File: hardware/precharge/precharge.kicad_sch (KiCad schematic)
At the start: 31 parts, among them J1 Conn_01x02, J2 Conn_01x01, J3 Conn_01x05, J4 Conn_01x04, J5 Conn_01x01, K1 DIPxx-1Cxx-51x, U1 140817141410, U2 140817141410, U3 140817141410

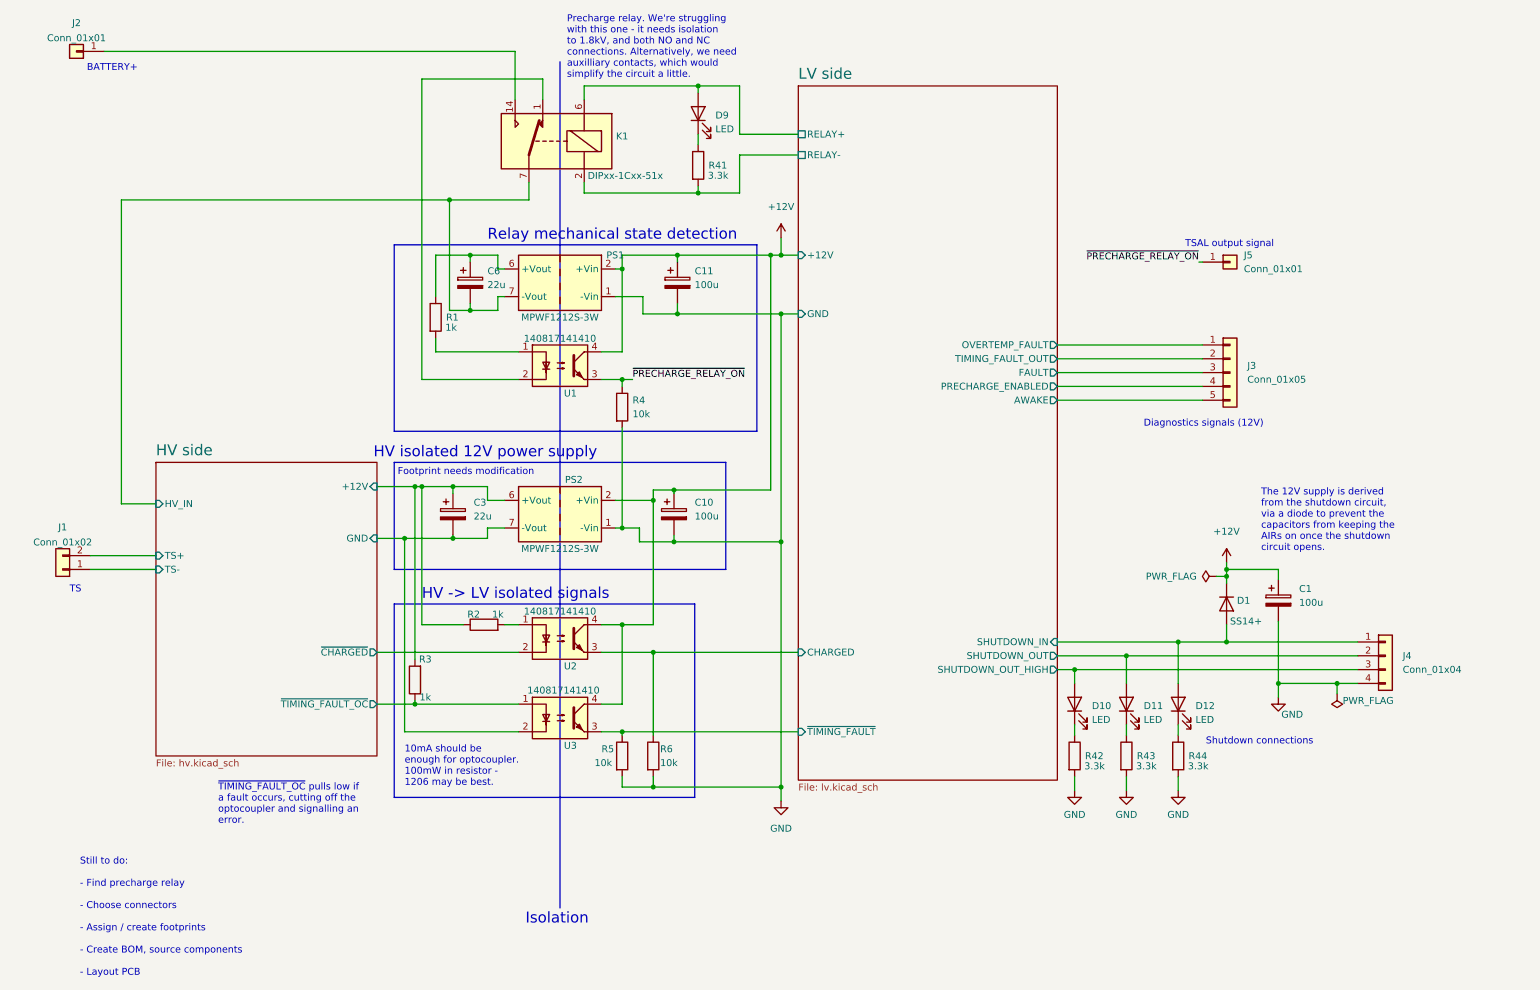
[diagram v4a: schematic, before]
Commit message: Added support for TS_ACTIVE signal, adjusted resistor divider
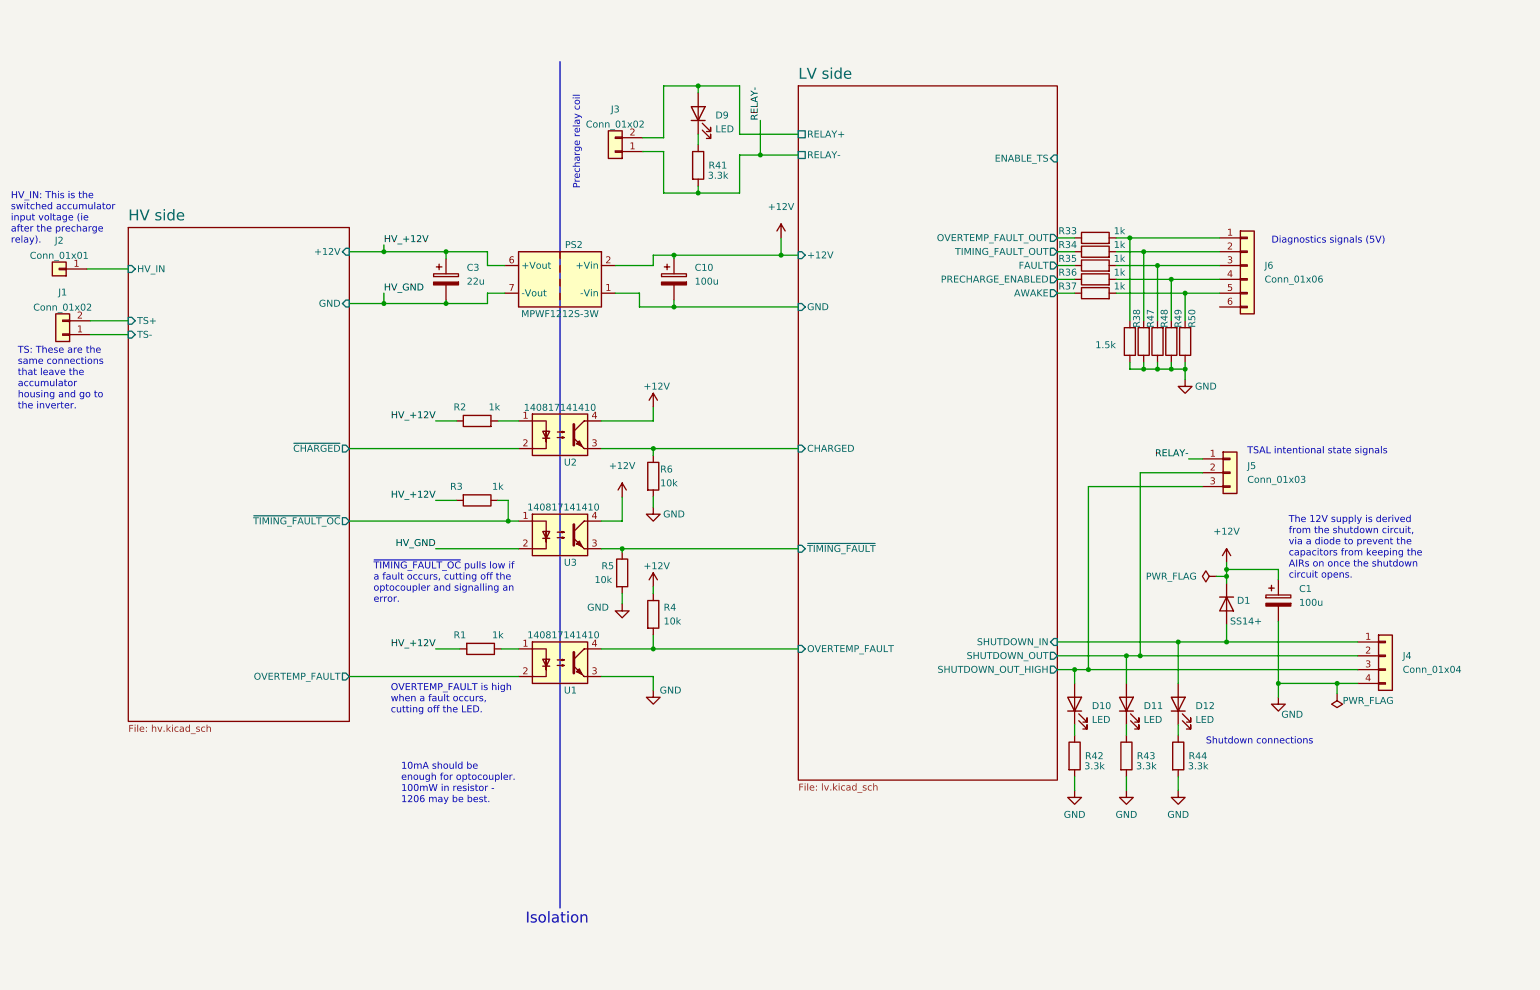
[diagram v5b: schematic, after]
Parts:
- removed C11: 100u, Capacitor_THT:CP_Radial_D6.3mm_P2.50mm, symbol Device:C_Polarized
- removed C6: 22u, Capacitor_THT:CP_Radial_D8.0mm_P3.50mm, symbol Device:C_Polarized
- removed J3: Conn_01x05, Connector_PinHeader_2.54mm:PinHeader_1x05_P2.54mm_Horizontal, symbol Connector_Generic:Conn_01x05
- removed J5: Conn_01x01, Connector_PinHeader_2.54mm:PinHeader_1x01_P2.54mm_Horizontal, symbol Connector_Generic:Conn_01x01
- removed K1: DIPxx-1Cxx-51x, Relay_THT:Relay_StandexMeder_DIP_LowProfile, symbol Relay:DIPxx-1Cxx-51x
- removed PS1: MPWF1212S-3W, Converter_DCDC:Converter_DCDC_XP_POWER-ITXxxxxSA_THT, symbol Converter_DCDC:ITX1212SA
- added J3: Conn_01x02, Connector_PinHeader_2.54mm:PinHeader_1x02_P2.54mm_Horizontal, symbol Connector_Generic:Conn_01x02
- added J5: Conn_01x03, Connector_PinHeader_2.54mm:PinHeader_1x03_P2.54mm_Horizontal, symbol Connector_Generic:Conn_01x03
- added J6: Conn_01x06, Connector_PinHeader_2.54mm:PinHeader_1x06_P2.54mm_Horizontal, symbol Connector_Generic:Conn_01x06
- added R33, R34, R35, R36, R37: 1k, Resistor_SMD:R_0603_1608Metric, symbol Device:R
- added R38, R47, R48, R49, R50: 1.5k, Resistor_SMD:R_0603_1608Metric, symbol Device:R
- R1: footprint Resistor_SMD:R_0603_1608Metric -> Resistor_SMD:R_1206_3216Metric; Power 2W -> (none)
- R2, R3: footprint Resistor_SMD:R_0603_1608Metric -> Resistor_SMD:R_1206_3216Metric
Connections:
- net HV side/+12V is gone; now on net HV_+12V: C3.1, PS2.6 (+Vout), R2.1, R3.2
- net +12V: now also R4.1; no longer U1.4
- net GND: now also U1.3, R38.1, R47.1, R48.1, R49.1, R50.1; no longer C10.2, PS2.1 (-Vin), R4.2
- net HV side/HV_IN: now also J2.1 (Pin_1)
- net LV side/AWAKE: now also R37.1
- net LV side/FAULT: now also R35.1
- net LV side/OVERTEMP_FAULT: now also R4.2, U1.4
- net LV side/PRECHARGE_ENABLED: now also R36.1
- net LV side/RELAY+: now also J3.2 (Pin_2)
- net LV side/SHUTDOWN_OUT: now also J5.2 (Pin_2)
- net LV side/SHUTDOWN_OUT_HIGH: now also J5.3 (Pin_3)
- net LV side/TIMING_FAULT_OUT: now also R34.1
- net at R1.1: now also U1.1
- net HV_+12V: now reaches R1.2
- net HV_+12V: no longer U1.1
- net HV side/OVERTEMP_FAULT: now reaches U1.2
- net HV side/GND renamed HV_GND
- net LV side/RELAY- renamed RELAY-
- net RELAY-: now also J3.1 (Pin_1), J5.1 (Pin_1)
- removed net ~{PRECHARGE_RELAY_ON}: R4.1, U1.3
- new net: J6.1 (Pin_1), R33.2, R38.2
- new net: J6.4 (Pin_4), R36.2, R49.2
- new net: J6.2 (Pin_2), R34.2, R47.2
- new net: J6.3 (Pin_3), R35.2, R48.2
- new net: J6.5 (Pin_5), R37.2, R50.2
- new net LV side/GND: C10.2, PS2.1 (-Vin)
- new net LV side/OVERTEMP_FAULT_OUT: R33.1
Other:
- sheet HV side ports: added OVERTEMP_FAULT; removed none
- sheet LV side ports: added ENABLE_TS, OVERTEMP_FAULT_OUT; removed none
- note added: "Diagnostics signals (5V)"
- note added: "HV_IN: This is the switched accumulator input voltage (ie after the precharge relay)."
- note added: "OVERTEMP_FAULT is high when a fault occurs, cutting off the LED."
- note added: "Precharge relay coil"
- note added: "TS: These are the same connections that leave the accumulator housing and go to the inverter."
- note added: "TSAL intentional state signals"
- note removed: "BATTERY+"
- note removed: "Diagnostics signals (12V)"
- note removed: "Footprint needs modification"
- note removed: "HV -> LV isolated signals"
- note removed: "HV isolated 12V power supply"
- note removed: "Precharge relay. We're struggling with this one - it needs isolation to 1.8kV, and both NO and NC connections. Alternatively, we need auxilliary contacts, which would simplify the circuit a little."
- note removed: "Relay mechanical state detection"
- note removed: "Still to do: - Find precharge relay - Choose connectors - Assign / create footprints - Create BOM, source components - Layout PCB"
- note removed: "TS"
- note removed: "TSAL output signal"
- moved on the sheet: C10, C3, J1, J2, PS2, R2, R3, R5, R6, U2, U3

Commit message: ??
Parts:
- removed J2: Conn_01x01, Connector_PinHeader_2.54mm:PinHeader_1x01_P2.54mm_Horizontal, symbol Connector_Generic:Conn_01x01
- removed J6: Conn_01x06, Connector_PinHeader_2.54mm:PinHeader_1x06_P2.54mm_Horizontal, symbol Connector_Generic:Conn_01x06
- added J2: Conn_01x02, Connector_Molex:Molex_Micro-Fit_3.0_43650-0200_1x02_P3.00mm_Horizontal, symbol Connector_Generic:Conn_01x02
- added J6: Conn_01x05, Connector_Molex:Molex_Micro-Fit_3.0_43650-0500_1x05_P3.00mm_Horizontal, symbol Connector_Generic:Conn_01x05
- J1, J3: footprint Connector_PinHeader_2.54mm:PinHeader_1x02_P2.54mm_Horizontal -> Connector_Molex:Molex_Micro-Fit_3.0_43650-0200_1x02_P3.00mm_Horizontal
- J4: footprint Connector_PinHeader_2.54mm:PinHeader_1x04_P2.54mm_Horizontal -> Connector_Molex:Molex_Micro-Fit_3.0_43650-0400_1x04_P3.00mm_Horizontal
- J5: footprint Connector_PinHeader_2.54mm:PinHeader_1x03_P2.54mm_Horizontal -> Connector_Molex:Molex_Micro-Fit_3.0_43650-0300_1x03_P3.00mm_Horizontal
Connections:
- net HV side/HV_IN: now also J2.1 (Pin_1), J2.2 (Pin_2)
- net at R33.2, R38.2: now also J6.1 (Pin_1)
- net at R36.2, R49.2: now also J6.4 (Pin_4)
- net at R34.2, R47.2: now also J6.2 (Pin_2)
- net at R35.2, R48.2: now also J6.3 (Pin_3)
- net at R37.2, R50.2: now also J6.5 (Pin_5)
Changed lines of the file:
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@@
   (junction (at 134.62 130.81) (diameter 0) (color 0 0 0 0)
+  )
+  (junction (at 31.75 60.96) (diameter 0) (color 0 0 0 0)
   )
   (junction (at 222.25 55.245) (diameter 0) (color 0 0 0 0)
@@
     (stroke (width 0) (type default) (color 0 0 0 0))
   )
+  (wire (pts (xy 30.48 58.42) (xy 31.75 58.42))
+    (stroke (width 0) (type default) (color 0 0 0 0))
+  )
   (wire (pts (xy 138.43 67.945) (xy 161.29 67.945))
     (stroke (width 0) (type default) (color 0 0 0 0))
@@
     (stroke (width 0) (type default) (color 0 0 0 0))
   )
-  (wire (pts (xy 30.48 60.96) (xy 38.1 60.96))
+  (wire (pts (xy 30.48 60.96) (xy 31.75 60.96))
     (stroke (width 0) (type default) (color 0 0 0 0))
   )
@@
     (stroke (width 0) (type default) (color 0 0 0 0))
   )
+  (wire (pts (xy 31.75 58.42) (xy 31.75 60.96))
+    (stroke (width 0) (type default) (color 0 0 0 0))
+  )
   (polyline (pts (xy 116.84 46.355) (xy 116.84 46.355))
     (stroke (width 0) (type default) (color 0 0 0 0))
@@
   )
   (wire (pts (xy 227.33 60.325) (xy 238.76 60.325))
+    (stroke (width 0) (type default) (color 0 0 0 0))
+  )
+  (wire (pts (xy 31.75 60.96) (xy 38.1 60.96))
     (stroke (width 0) (type default) (color 0 0 0 0))
   )
@@
   )
   (text "HV_IN: This is the\nswitched accumulator\ninput voltage (ie \nafter the precharge\nrelay)."
-    (at 16.51 56.515 0)
+    (at 16.51 48.895 0)
     (effects (font (size 1.27 1.27)) (justify left bottom))
   )
@@
     (pin "2")
   )
+  (symbol (lib_id "Connector_Generic:Conn_01x05") (at 243.84 60.325 0) (unit 1)
+    (in_bom yes) (on_board yes) (fields_autoplaced)
+    (property "Reference" "J6" (id 0) (at 246.38 59.0549 0)
+      (effects (font (size 1.27 1.27)) (justify left))
+    )
+    (property "Value" "Conn_01x05" (id 1) (at 246.38 61.5949 0)
+      (effects (font (size 1.27 1.27)) (justify left))
+    )
+    (property "Footprint" "Connector_Molex:Molex_Micro-Fit_3.0_43650-0500_1x05_P3.00mm_Horizontal" (id 2) (at 243.84 60.325 0)
+      (effects (font (size 1.27 1.27)) hide)
+    )
+    (property "Datasheet" "~" (id 3) (at 243.84 60.325 0)
+      (effects (font (size 1.27 1.27)) hide)
+    )
+    (pin "1")
+    (pin "2")
+    (pin "3")
+    (pin "4")
+    (pin "5")
+  )
   (symbol (lib_id "Device:R") (at 212.09 150.495 0) (unit 1)
     (in_bom yes) (on_board yes)
@@
     (pin "2")
   )
-  (symbol (lib_id "Connector_Generic:Conn_01x06") (at 243.84 60.325 0) (unit 1)
-    (in_bom yes) (on_board yes) (fields_autoplaced)
-    (property "Reference" "J6" (id 0) (at 247.015 60.3249 0)
-      (effects (font (size 1.27 1.27)) (justify left))
-    )
-    (property "Value" "Conn_01x06" (id 1) (at 247.015 62.8649 0)
-      (effects (font (size 1.27 1.27)) (justify left))
-    )
-    (property "Footprint" "Connector_PinHeader_2.54mm:PinHeader_1x06_P2.54mm_Horizontal" (id 2) (at 243.84 60.325 0)
-      (effects (font (size 1.27 1.27)) hide)
-    )
-    (property "Datasheet" "~" (id 3) (at 243.84 60.325 0)
-      (effects (font (size 1.27 1.27)) hide)
-    )
-    (pin "1")
-    (pin "2")
-    (pin "3")
-    (pin "4")
-    (pin "5")
-    (pin "6")
+  (symbol (lib_id "Connector_Generic:Conn_01x02") (at 25.4 60.96 180) (unit 1)
+    (in_bom yes) (on_board yes) (fields_autoplaced)
+    (property "Reference" "J2" (id 0) (at 25.4 51.435 0))
+    (property "Value" "Conn_01x02" (id 1) (at 25.4 53.975 0))
+    (property "Footprint" "Connector_Molex:Molex_Micro-Fit_3.0_43650-0200_1x02_P3.00mm_Horizontal" (id 2) (at 25.4 60.96 0)
+      (effects (font (size 1.27 1.27)) hide)
+    )
+    (property "Datasheet" "~" (id 3) (at 25.4 60.96 0)
+      (effects (font (size 1.27 1.27)) hide)
+    )
+    (pin "1")
+    (pin "2")
   )
   (symbol (lib_id "power:+12V") (at 128.905 102.87 0) (unit 1)
@@
       (effects (font (size 1.27 1.27)) (justify left))
     )
-    (property "Footprint" "Connector_PinHeader_2.54mm:PinHeader_1x04_P2.54mm_Horizontal" (id 2) (at 269.24 132.08 0)
+    (property "Footprint" "Connector_Molex:Molex_Micro-Fit_3.0_43650-0400_1x04_P3.00mm_Horizontal" (id 2) (at 269.24 132.08 0)
       (effects (font (size 1.27 1.27)) hide)
     )
@@
     (pin "1")
   )
-  (symbol (lib_id "Connector_Generic:Conn_01x01") (at 25.4 60.96 180) (unit 1)
-    (in_bom yes) (on_board yes) (fields_autoplaced)
-    (property "Reference" "J2" (id 0) (at 25.4 55.7235 0))
-    (property "Value" "Conn_01x01" (id 1) (at 25.4 58.4986 0))
-    (property "Footprint" "Connector_PinHeader_2.54mm:PinHeader_1x01_P2.54mm_Horizontal" (id 2) (at 25.4 60.96 0)
-      (effects (font (size 1.27 1.27)) hide)
-    )
-    (property "Datasheet" "~" (id 3) (at 25.4 60.96 0)
-      (effects (font (size 1.27 1.27)) hide)
-    )
-    (pin "1")
-  )
   (symbol (lib_id "Device:C_Polarized") (at 96.52 62.865 0) (unit 1)
     (in_bom yes) (on_board yes) (fields_autoplaced)
@@
     (property "Reference" "J3" (id 0) (at 127.635 31.5935 0))
     (property "Value" "Conn_01x02" (id 1) (at 127.635 34.3686 0))
-    (property "Footprint" "Connector_PinHeader_2.54mm:PinHeader_1x02_P2.54mm_Horizontal" (id 2) (at 127.635 39.37 0)
+    (property "Footprint" "Connector_Molex:Molex_Micro-Fit_3.0_43650-0200_1x02_P3.00mm_Horizontal" (id 2) (at 127.635 39.37 0)
       (effects (font (size 1.27 1.27)) hide)
     )
@@
       (effects (font (size 1.27 1.27)) (justify left))
     )
-    (property "Footprint" "Connector_PinHeader_2.54mm:PinHeader_1x03_P2.54mm_Horizontal" (id 2) (at 240.665 98.425 0)
+    (property "Footprint" "Connector_Molex:Molex_Micro-Fit_3.0_43650-0300_1x03_P3.00mm_Horizontal" (id 2) (at 240.665 98.425 0)
       (effects (font (size 1.27 1.27)) hide)
     )
@@
     (property "Reference" "J1" (id 0) (at 26.035 65.2485 0))
     (property "Value" "Conn_01x02" (id 1) (at 26.035 68.0236 0))
-    (property "Footprint" "Connector_PinHeader_2.54mm:PinHeader_1x02_P2.54mm_Horizontal" (id 2) (at 26.035 73.025 0)
+    (property "Footprint" "Connector_Molex:Molex_Micro-Fit_3.0_43650-0200_1x02_P3.00mm_Horizontal" (id 2) (at 26.035 73.025 0)
       (effects (font (size 1.27 1.27)) hide)
     )
@@
     )
     (path "/c1d028f3-91e9-41f8-8563-411af756b606"
-      (reference "J1") (unit 1) (value "Conn_01x02") (footprint "Connector_PinHeader_2.54mm:PinHeader_1x02_P2.54mm_Horizontal")
-    )
-    (path "/9675ae6d-9635-4b89-ab4f-854f5484396b"
-      (reference "J2") (unit 1) (value "Conn_01x01") (footprint "Connector_PinHeader_2.54mm:PinHeader_1x01_P2.54mm_Horizontal")
+      (reference "J1") (unit 1) (value "Conn_01x02") (footprint "Connector_Molex:Molex_Micro-Fit_3.0_43650-0200_1x02_P3.00mm_Horizontal")
+    )
+    (path "/42f26f97-84ba-4654-93f0-c5bfb573e97d"
+      (reference "J2") (unit 1) (value "Conn_01x02") (footprint "Connector_Molex:Molex_Micro-Fit_3.0_43650-0200_1x02_P3.00mm_Horizontal")
     )
     (path "/ac2f3eb5-9193-4a6c-bab6-d1de91fe5122"
-      (reference "J3") (unit 1) (value "Conn_01x02") (footprint "Connector_PinHeader_2.54mm:PinHeader_1x02_P2.54mm_Horizontal")
+      (reference "J3") (unit 1) (value "Conn_01x02") (footprint "Connector_Molex:Molex_Micro-Fit_3.0_43650-0200_1x02_P3.00mm_Horizontal")
     )
     (path "/616c1ff6-bb93-43c9-a485-6175455d841d"
-      (reference "J4") (unit 1) (value "Conn_01x04") (footprint "Connector_PinHeader_2.54mm:PinHeader_1x04_P2.54mm_Horizontal")
+      (reference "J4") (unit 1) (value "Conn_01x04") (footprint "Connector_Molex:Molex_Micro-Fit_3.0_43650-0400_1x04_P3.00mm_Horizontal")
     )
     (path "/bec1f211-1161-41c0-a581-e039a5c66ab7"
-      (reference "J5") (unit 1) (value "Conn_01x03") (footprint "Connector_PinHeader_2.54mm:PinHeader_1x03_P2.54mm_Horizontal")
-    )
-    (path "/45401762-23c2-4a87-8d43-c8f6f1d0d8c3"
-      (reference "J6") (unit 1) (value "Conn_01x06") (footprint "Connector_PinHeader_2.54mm:PinHeader_1x06_P2.54mm_Horizontal")
+      (reference "J5") (unit 1) (value "Conn_01x03") (footprint "Connector_Molex:Molex_Micro-Fit_3.0_43650-0300_1x03_P3.00mm_Horizontal")
+    )
+    (path "/1a1ae468-a772-4e3f-8cb1-1536f03ea476"
+      (reference "J6") (unit 1) (value "Conn_01x05") (footprint "Connector_Molex:Molex_Micro-Fit_3.0_43650-0500_1x05_P3.00mm_Horizontal")
     )
     (path "/a25b3faf-d95a-49ad-9b40-7c3f8d869233/0eaa663a-c98d-44db-8bf5-70ab2ac22caf"

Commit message: ??
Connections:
- net LV side/PRECHARGE_ENABLED: now also J5.1 (Pin_1)
- net RELAY- renamed LV side/RELAY-
- net LV side/RELAY-: no longer J5.1 (Pin_1)
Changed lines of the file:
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@@
   (junction (at 231.14 129.54) (diameter 0) (color 0 0 0 0)
   )
+  (junction (at 210.82 62.865) (diameter 0) (color 0 0 0 0)
+  )
   (junction (at 138.43 67.945) (diameter 0) (color 0 0 0 0)
   )
@@
   (junction (at 240.03 129.54) (diameter 0) (color 0 0 0 0)
   )
-  (junction (at 154.305 40.005) (diameter 0) (color 0 0 0 0)
-  )
   (junction (at 229.87 62.865) (diameter 0) (color 0 0 0 0)
   )
@@
   )
   (wire (pts (xy 222.25 55.245) (xy 238.76 55.245))
+    (stroke (width 0) (type default) (color 0 0 0 0))
+  )
+  (wire (pts (xy 210.82 62.865) (xy 212.09 62.865))
     (stroke (width 0) (type default) (color 0 0 0 0))
   )
@@
     (stroke (width 0) (type default) (color 0 0 0 0))
   )
-  (wire (pts (xy 150.495 40.005) (xy 154.305 40.005))
-    (stroke (width 0) (type default) (color 0 0 0 0))
-  )
   (wire (pts (xy 219.71 62.865) (xy 229.87 62.865))
     (stroke (width 0) (type default) (color 0 0 0 0))
@@
     (stroke (width 0) (type default) (color 0 0 0 0))
   )
-  (wire (pts (xy 154.305 33.655) (xy 154.305 40.005))
-    (stroke (width 0) (type default) (color 0 0 0 0))
-  )
   (wire (pts (xy 134.62 58.42) (xy 138.43 58.42))
     (stroke (width 0) (type default) (color 0 0 0 0))
@@
     (stroke (width 0) (type default) (color 0 0 0 0))
   )
-  (wire (pts (xy 233.045 95.885) (xy 235.585 95.885))
+  (wire (pts (xy 210.82 95.885) (xy 235.585 95.885))
     (stroke (width 0) (type default) (color 0 0 0 0))
   )
@@
     (stroke (width 0) (type default) (color 0 0 0 0))
   )
-  (wire (pts (xy 208.915 62.865) (xy 212.09 62.865))
+  (wire (pts (xy 208.915 62.865) (xy 210.82 62.865))
     (stroke (width 0) (type default) (color 0 0 0 0))
   )
@@
     (stroke (width 0) (type default) (color 0 0 0 0))
   )
+  (wire (pts (xy 210.82 95.885) (xy 210.82 62.865))
+    (stroke (width 0) (type default) (color 0 0 0 0))
+  )
   (wire (pts (xy 208.915 134.62) (xy 212.09 134.62))
     (stroke (width 0) (type default) (color 0 0 0 0))
@@
     (stroke (width 0) (type default) (color 0 0 0 0))
   )
-  (wire (pts (xy 154.305 40.005) (xy 161.29 40.005))
+  (wire (pts (xy 150.495 40.005) (xy 161.29 40.005))
     (stroke (width 0) (type default) (color 0 0 0 0))
   )
@@
     (effects (font (size 1.27 1.27)) (justify left bottom))
   )
-  (label "RELAY-" (at 233.045 95.885 180)
-    (effects (font (size 1.27 1.27)) (justify right bottom))
-  )
   (label "HV_+12V" (at 94.615 130.81 180)
     (effects (font (size 1.27 1.27)) (justify right bottom))
@@
     (effects (font (size 1.27 1.27)) (justify left bottom))
   )
-  (label "RELAY-" (at 154.305 33.655 90)
-    (effects (font (size 1.27 1.27)) (justify left bottom))
-  )
